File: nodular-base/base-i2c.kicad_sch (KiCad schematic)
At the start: 2 parts, among them U4 TCA9548APWR, U7 SC7A20

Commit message: WIP layout for base
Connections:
- net SDA_C: now reaches U4.10 (SD3)
- net SCL_C: now reaches U4.11 (SC3)
- net GND: now reaches U4.12 (GND)
- net SDA_D: now reaches U4.13 (SD4)
- net SCL_D: now reaches U4.14 (SC4)
- net SDA_E: now reaches U4.15 (SD5)
- net SCL_E: now reaches U4.16 (SC5)
- net SDA_F: now reaches U4.17 (SD6)
- net SCL_F: now reaches U4.18 (SC6)
- net SDA_SYS: now reaches U4.4 (SD0)
- net SCL_SYS: now reaches U4.5 (SC0)
- net SDA_A: now reaches U4.6 (SD1)
- net SCL_A: now reaches U4.7 (SC1)
- net SDA_B: now reaches U4.8 (SD2)
- net SCL_B: now reaches U4.9 (SC2)
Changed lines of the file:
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@@
 (kicad_sch (version 20230121) (generator eeschema)
   (paper "A4")
+  (hierarchical_label "SCL_E" (shape output) (at 123.19 82.55 0) (fields_autoplaced)
+    (effects (font (size 1.27 1.27)) (justify left))
+  )
+  (hierarchical_label "SDA_D" (shape bidirectional) (at 123.19 80.01 0) (fields_autoplaced)
+    (effects (font (size 1.27 1.27)) (justify left))
+  )
+  (hierarchical_label "SCL_SYS" (shape output) (at 123.19 57.15 0) (fields_autoplaced)
+    (effects (font (size 1.27 1.27)) (justify left))
+  )
+  (hierarchical_label "SCL_F" (shape output) (at 123.19 87.63 0) (fields_autoplaced)
+    (effects (font (size 1.27 1.27)) (justify left))
+  )
+  (hierarchical_label "SDA_B" (shape bidirectional) (at 123.19 69.85 0) (fields_autoplaced)
+    (effects (font (size 1.27 1.27)) (justify left))
+  )
+  (hierarchical_label "SCL_B" (shape output) (at 123.19 67.31 0) (fields_autoplaced)
+    (effects (font (size 1.27 1.27)) (justify left))
+  )
+  (hierarchical_label "SDA_C" (shape bidirectional) (at 123.19 74.93 0) (fields_autoplaced)
+    (effects (font (size 1.27 1.27)) (justify left))
+  )
+  (hierarchical_label "SDA_F" (shape bidirectional) (at 123.19 90.17 0) (fields_autoplaced)
+    (effects (font (size 1.27 1.27)) (justify left))
+  )
+  (hierarchical_label "SCL_C" (shape output) (at 123.19 72.39 0) (fields_autoplaced)
+    (effects (font (size 1.27 1.27)) (justify left))
+  )
+  (hierarchical_label "SDA_A" (shape bidirectional) (at 123.19 64.77 0) (fields_autoplaced)
+    (effects (font (size 1.27 1.27)) (justify left))
+  )
+  (hierarchical_label "SDA_SYS" (shape bidirectional) (at 123.19 59.69 0) (fields_autoplaced)
+    (effects (font (size 1.27 1.27)) (justify left))
+  )
+  (hierarchical_label "SCL_D" (shape output) (at 123.19 77.47 0) (fields_autoplaced)
+    (effects (font (size 1.27 1.27)) (justify left))
+  )
+  (hierarchical_label "SDA_E" (shape bidirectional) (at 123.19 85.09 0) (fields_autoplaced)
+    (effects (font (size 1.27 1.27)) (justify left))
+  )
+  (hierarchical_label "SCL_A" (shape output) (at 123.19 62.23 0) (fields_autoplaced)
+    (effects (font (size 1.27 1.27)) (justify left))
+  )
   (symbol (lib_id "Interface_Expansion:TCA9548APWR") (at 113.03 74.93 0) (unit 1)
     (in_bom yes) (on_board yes) (dnp no) (fields_autoplaced)
@@
         )
       )
+    )
+  )
+  (symbol (lib_id "power:GND") (at 113.03 100.33 0) (unit 1)
+    (in_bom yes) (on_board yes) (dnp no) (fields_autoplaced)
+    (property "Reference" "#PWR042" (at 113.03 106.68 0)
+      (effects (font (size 1.27 1.27)) hide)
+    )
+    (property "Value" "GND" (at 113.03 105.41 0)
+      (effects (font (size 1.27 1.27)))
+    )
+    (property "Footprint" "" (at 113.03 100.33 0)
+      (effects (font (size 1.27 1.27)) hide)
+    )
+    (property "Datasheet" "" (at 113.03 100.33 0)
+      (effects (font (size 1.27 1.27)) hide)
+    )
+    (pin "1")
+    (instances
+      (project "nodular-base"
+        (path "/6dcb0502-87e2-4c28-9ce8-81aab8925f06/5ae693f9-48f3-406c-bbdf-b76d81cc71eb"
+          (reference "#PWR042") (unit 1)
+        )
+      )

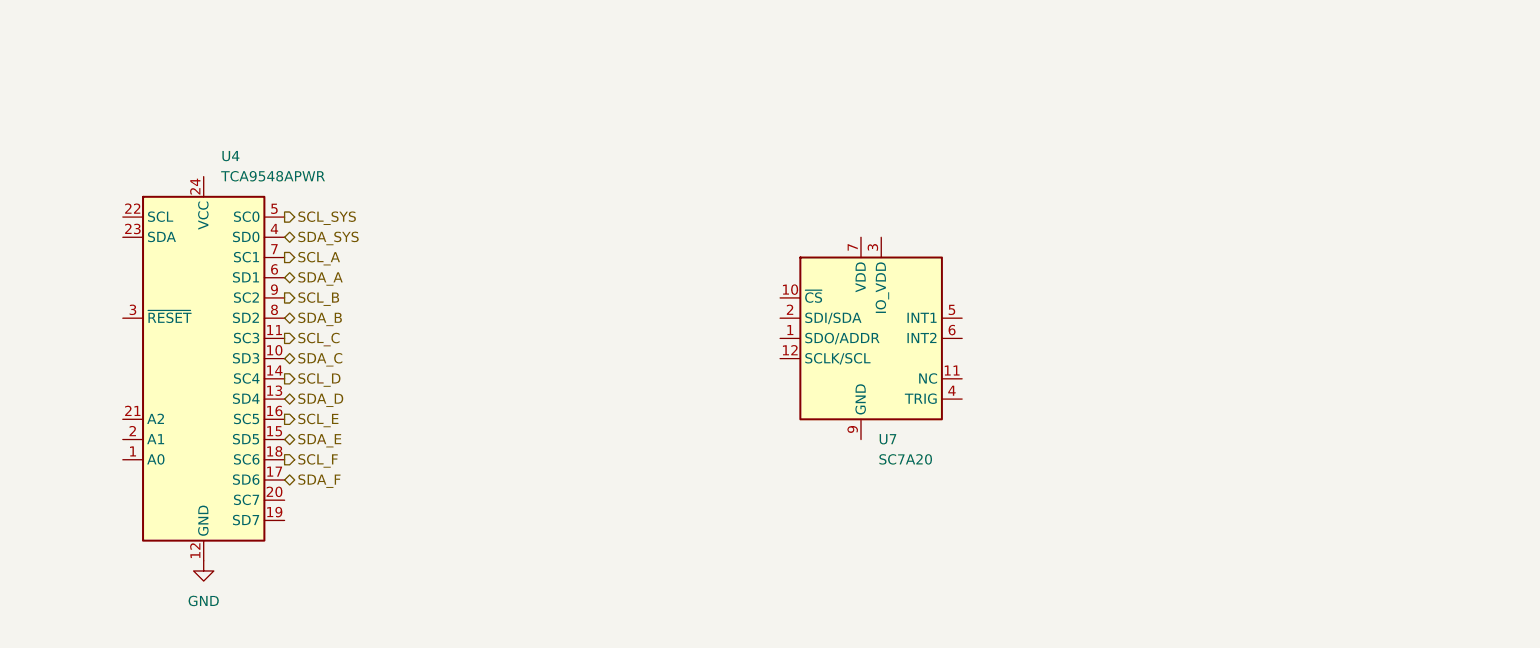
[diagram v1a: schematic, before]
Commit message: Switched from CAN to USB for second USB-C port Added second PD controller and USB mux to allow switching between host and device port Added SOICbite to corner All routing complete Updated pin map, added i2c addresses, soicbit pin mapping, and fpc pinout to document
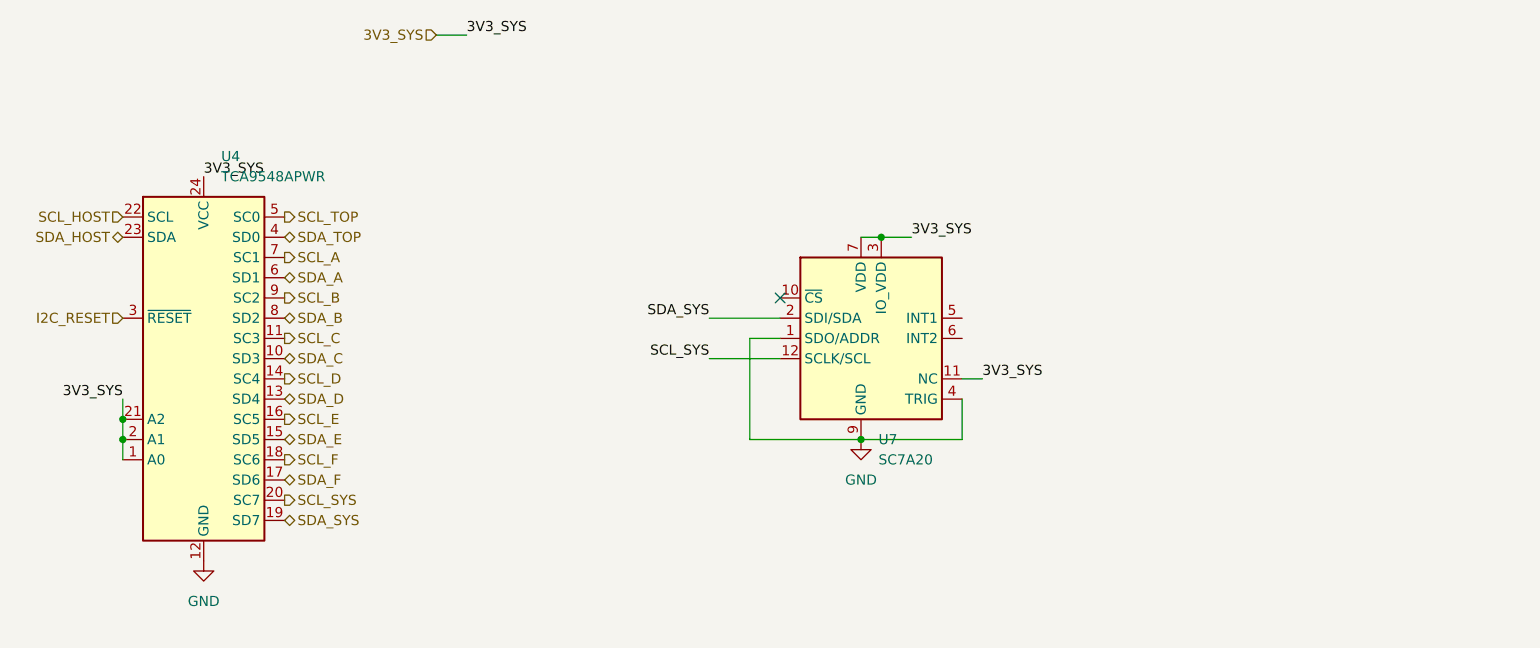
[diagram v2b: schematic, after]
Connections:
- net GND: now also U7.1 (SDO/ADDR), U7.4 (TRIG), U7.9 (GND)
- net SCL_SYS: now also U4.20 (SC7), U7.12 (SCLK/SCL); no longer U4.5 (SC0)
- net SDA_SYS: now also U4.19 (SD7), U7.2 (SDI/SDA); no longer U4.4 (SD0)
- net 3V3_SYS: now reaches U4.1 (A0)
- net 3V3_SYS: now also U4.2 (A1), U4.21 (A2), U4.24 (VCC), U7.11 (NC), U7.3 (IO_VDD), U7.7 (VDD)
- net SCL_HOST: now reaches U4.22 (SCL)
- net SDA_HOST: now reaches U4.23 (SDA)
- net I2C_RESET: now reaches U4.3 (~{RESET})
- new net SCL_TOP: U4.5 (SC0)
- new net SDA_TOP: U4.4 (SD0)
- no-connect marks 0 -> 1
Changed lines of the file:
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@@
 (kicad_sch (version 20230121) (generator eeschema)
   (paper "A4")
+  (junction (at 102.87 85.09) (diameter 0) (color 0 0 0 0)
+  )
+  (junction (at 102.87 82.55) (diameter 0) (color 0 0 0 0)
+  )
+  (junction (at 198.12 59.69) (diameter 0) (color 0 0 0 0)
+  )
+  (junction (at 195.58 85.09) (diameter 0) (color 0 0 0 0)
+  )
+  (no_connect (at 185.42 67.31))
+  (wire (pts (xy 102.87 82.55) (xy 102.87 85.09))
+    (stroke (width 0) (type default))
+  )
+  (wire (pts (xy 198.12 59.69) (xy 201.93 59.69))
+    (stroke (width 0) (type default))
+  )
+  (wire (pts (xy 176.53 74.93) (xy 185.42 74.93))
+    (stroke (width 0) (type default))
+  )
+  (wire (pts (xy 208.28 85.09) (xy 195.58 85.09))
+    (stroke (width 0) (type default))
+  )
+  (wire (pts (xy 176.53 69.85) (xy 185.42 69.85))
+    (stroke (width 0) (type default))
+  )
+  (wire (pts (xy 102.87 80.01) (xy 102.87 82.55))
+    (stroke (width 0) (type default))
+  )
+  (wire (pts (xy 181.61 85.09) (xy 195.58 85.09))
+    (stroke (width 0) (type default))
+  )
+  (wire (pts (xy 195.58 59.69) (xy 198.12 59.69))
+    (stroke (width 0) (type default))
+  )
+  (wire (pts (xy 181.61 72.39) (xy 181.61 85.09))
+    (stroke (width 0) (type default))
+  )
+  (wire (pts (xy 185.42 72.39) (xy 181.61 72.39))
+    (stroke (width 0) (type default))
+  )
+  (wire (pts (xy 102.87 85.09) (xy 102.87 87.63))
+    (stroke (width 0) (type default))
+  )
+  (wire (pts (xy 208.28 77.47) (xy 210.82 77.47))
+    (stroke (width 0) (type default))
+  )
+  (wire (pts (xy 208.28 80.01) (xy 208.28 85.09))
+    (stroke (width 0) (type default))
+  )
+  (wire (pts (xy 142.24 34.29) (xy 146.05 34.29))
+    (stroke (width 0) (type default))
+  )
+  (label "3V3_SYS" (at 113.03 52.07 0) (fields_autoplaced)
+    (effects (font (size 1.27 1.27)) (justify left bottom))
+  )
+  (label "SCL_SYS" (at 176.53 74.93 180) (fields_autoplaced)
+    (effects (font (size 1.27 1.27)) (justify right bottom))
+  )
+  (label "3V3_SYS" (at 102.87 80.01 180) (fields_autoplaced)
+    (effects (font (size 1.27 1.27)) (justify right bottom))
+  )
+  (label "3V3_SYS" (at 201.93 59.69 0) (fields_autoplaced)
+    (effects (font (size 1.27 1.27)) (justify left bottom))
+  )
+  (label "3V3_SYS" (at 210.82 77.47 0) (fields_autoplaced)
+    (effects (font (size 1.27 1.27)) (justify left bottom))
+  )
+  (label "SDA_SYS" (at 176.53 69.85 180) (fields_autoplaced)
+    (effects (font (size 1.27 1.27)) (justify right bottom))
+  )
+  (label "3V3_SYS" (at 146.05 34.29 0) (fields_autoplaced)
+    (effects (font (size 1.27 1.27)) (justify left bottom))
+  )
+  (hierarchical_label "3V3_SYS" (shape input) (at 142.24 34.29 180) (fields_autoplaced)
+    (effects (font (size 1.27 1.27)) (justify right))
+  )
   (hierarchical_label "SCL_E" (shape output) (at 123.19 82.55 0) (fields_autoplaced)
     (effects (font (size 1.27 1.27)) (justify left))
@@
     (effects (font (size 1.27 1.27)) (justify left))
   )
-  (hierarchical_label "SCL_SYS" (shape output) (at 123.19 57.15 0) (fields_autoplaced)
+  (hierarchical_label "SDA_HOST" (shape bidirectional) (at 102.87 59.69 180) (fields_autoplaced)
+    (effects (font (size 1.27 1.27)) (justify right))
+  )
+  (hierarchical_label "SCL_SYS" (shape output) (at 123.19 92.71 0) (fields_autoplaced)
     (effects (font (size 1.27 1.27)) (justify left))
   )
@@
     (effects (font (size 1.27 1.27)) (justify left))
   )
+  (hierarchical_label "I2C_RESET" (shape input) (at 102.87 69.85 180) (fields_autoplaced)
+    (effects (font (size 1.27 1.27)) (justify right))
+  )
   (hierarchical_label "SCL_B" (shape output) (at 123.19 67.31 0) (fields_autoplaced)
     (effects (font (size 1.27 1.27)) (justify left))
@@
     (effects (font (size 1.27 1.27)) (justify left))
   )
+  (hierarchical_label "SCL_HOST" (shape input) (at 102.87 57.15 180) (fields_autoplaced)
+    (effects (font (size 1.27 1.27)) (justify right))
+  )
+  (hierarchical_label "SCL_TOP" (shape output) (at 123.19 57.15 0) (fields_autoplaced)
+    (effects (font (size 1.27 1.27)) (justify left))
+  )
   (hierarchical_label "SDA_F" (shape bidirectional) (at 123.19 90.17 0) (fields_autoplaced)
     (effects (font (size 1.27 1.27)) (justify left))
@@
     (effects (font (size 1.27 1.27)) (justify left))
   )
-  (hierarchical_label "SDA_SYS" (shape bidirectional) (at 123.19 59.69 0) (fields_autoplaced)
+  (hierarchical_label "SDA_SYS" (shape bidirectional) (at 123.19 95.25 0) (fields_autoplaced)
     (effects (font (size 1.27 1.27)) (justify left))
   )
@@
   )
   (hierarchical_label "SDA_E" (shape bidirectional) (at 123.19 85.09 0) (fields_autoplaced)
+    (effects (font (size 1.27 1.27)) (justify left))
+  )
+  (hierarchical_label "SDA_TOP" (shape bidirectional) (at 123.19 59.69 0) (fields_autoplaced)
     (effects (font (size 1.27 1.27)) (justify left))
   )
@@
         )
       )
+    )
+  )
+  (symbol (lib_id "power:GND") (at 195.58 85.09 0) (unit 1)
+    (in_bom yes) (on_board yes) (dnp no) (fields_autoplaced)
+    (property "Reference" "#PWR050" (at 195.58 91.44 0)
+      (effects (font (size 1.27 1.27)) hide)
+    )
+    (property "Value" "GND" (at 195.58 90.17 0)
+      (effects (font (size 1.27 1.27)))
+    )
+    (property "Footprint" "" (at 195.58 85.09 0)
+      (effects (font (size 1.27 1.27)) hide)
+    )
+    (property "Datasheet" "" (at 195.58 85.09 0)
+      (effects (font (size 1.27 1.27)) hide)
+    )
+    (pin "1")
+    (instances
+      (project "nodular-base"
+        (path "/6dcb0502-87e2-4c28-9ce8-81aab8925f06/5ae693f9-48f3-406c-bbdf-b76d81cc71eb"
+          (reference "#PWR050") (unit 1)
+        )
+      )

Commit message: Add hole Add decoupling caps, pullups, and voltage dividers Set current limit on PMIC Determine battery attachment angle Update BOM and pinouts
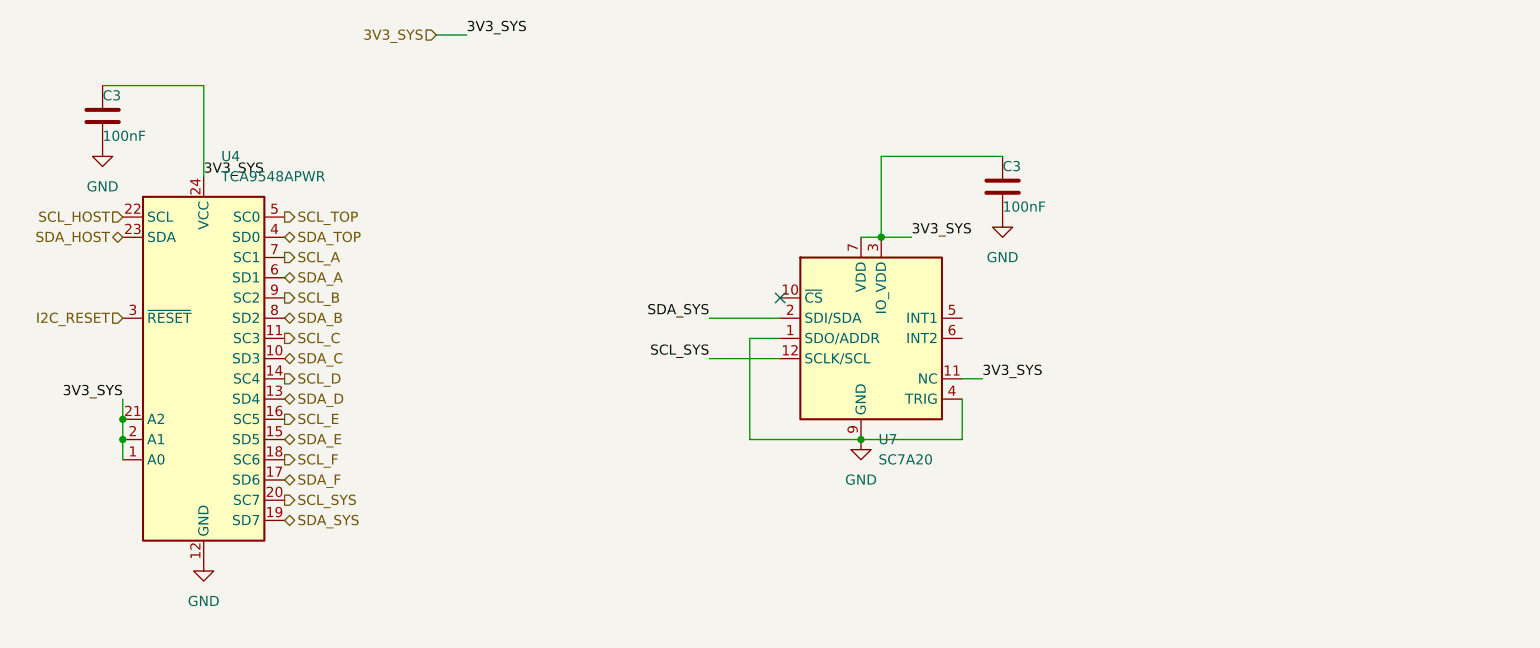
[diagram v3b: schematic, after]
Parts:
- added C3 (x2): 100nF, Capacitor_SMD:C_0402_1005Metric, symbol Device:C
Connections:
- net 3V3_SYS: now also C3.1, C3.1
- net GND: now also C3.2, C3.2
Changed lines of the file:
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@@
+    (stroke (width 0) (type default))
+  )
+  (wire (pts (xy 113.03 40.64) (xy 100.33 40.64))
     (stroke (width 0) (type default))
   )
@@
     (stroke (width 0) (type default))
   )
+  (wire (pts (xy 213.36 49.53) (xy 198.12 49.53))
+    (stroke (width 0) (type default))
+  )
   (wire (pts (xy 102.87 80.01) (xy 102.87 82.55))
     (stroke (width 0) (type default))
@@
     (stroke (width 0) (type default))
   )
+  (wire (pts (xy 113.03 52.07) (xy 113.03 40.64))
+    (stroke (width 0) (type default))
+  )
   (wire (pts (xy 195.58 59.69) (xy 198.12 59.69))
+    (stroke (width 0) (type default))
+  )
+  (wire (pts (xy 198.12 49.53) (xy 198.12 59.69))
     (stroke (width 0) (type default))
   )
@@
     )
   )
+  (symbol (lib_id "Device:C") (at 213.36 53.34 0) (unit 1)
+    (in_bom yes) (on_board yes) (dnp no)
+    (property "Reference" "C3" (at 213.36 50.8 0)
+      (effects (font (size 1.27 1.27)) (justify left))
+    )
+    (property "Value" "100nF" (at 213.36 55.88 0)
+      (effects (font (size 1.27 1.27)) (justify left))
+    )
+    (property "Footprint" "Capacitor_SMD:C_0402_1005Metric" (at 214.3252 57.15 0)
+      (effects (font (size 1.27 1.27)) hide)
+    )
+    (property "Datasheet" "~" (at 213.36 53.34 0)
+      (effects (font (size 1.27 1.27)) hide)
+    )
+    (pin "1")
+    (pin "2")
+    (instances
+      (project "nodular-base"
+        (path "/6dcb0502-87e2-4c28-9ce8-81aab8925f06"
+          (reference "C3") (unit 1)
+        )
+        (path "/6dcb0502-87e2-4c28-9ce8-81aab8925f06/5ae693f9-48f3-406c-bbdf-b76d81cc71eb"
+          (reference "C42") (unit 1)
+        )
+      )
+    )
+  )
+  (symbol (lib_id "Device:C") (at 100.33 44.45 0) (unit 1)
+    (in_bom yes) (on_board yes) (dnp no)
+    (property "Reference" "C3" (at 100.33 41.91 0)
+      (effects (font (size 1.27 1.27)) (justify left))
+    )
+    (property "Value" "100nF" (at 100.33 46.99 0)
+      (effects (font (size 1.27 1.27)) (justify left))
+    )
+    (property "Footprint" "Capacitor_SMD:C_0402_1005Metric" (at 101.2952 48.26 0)
+      (effects (font (size 1.27 1.27)) hide)
+    )
+    (property "Datasheet" "~" (at 100.33 44.45 0)
+      (effects (font (size 1.27 1.27)) hide)
+    )
+    (pin "1")
+    (pin "2")
+    (instances
+      (project "nodular-base"
+        (path "/6dcb0502-87e2-4c28-9ce8-81aab8925f06"
+          (reference "C3") (unit 1)
+        )
+        (path "/6dcb0502-87e2-4c28-9ce8-81aab8925f06/5ae693f9-48f3-406c-bbdf-b76d81cc71eb"
+          (reference "C16") (unit 1)
+        )
+      )
+    )
+  )
+  (symbol (lib_id "power:GND") (at 213.36 57.15 0) (unit 1)
+    (in_bom yes) (on_board yes) (dnp no) (fields_autoplaced)
+    (property "Reference" "#PWR061" (at 213.36 63.5 0)
+      (effects (font (size 1.27 1.27)) hide)
+    )
+    (property "Value" "GND" (at 213.36 62.23 0)
+      (effects (font (size 1.27 1.27)))
+    )
+    (property "Footprint" "" (at 213.36 57.15 0)
+      (effects (font (size 1.27 1.27)) hide)
+    )
+    (property "Datasheet" "" (at 213.36 57.15 0)
+      (effects (font (size 1.27 1.27)) hide)
+    )
+    (pin "1")
+    (instances
+      (project "nodular-base"
+        (path "/6dcb0502-87e2-4c28-9ce8-81aab8925f06/5ae693f9-48f3-406c-bbdf-b76d81cc71eb"
+          (reference "#PWR061") (unit 1)
+        )
+      )
+    )
+  )
   (symbol (lib_id "power:GND") (at 195.58 85.09 0) (unit 1)
     (in_bom yes) (on_board yes) (dnp no) (fields_autoplaced)
@@
         )
       )
+    )
+  )
+  (symbol (lib_id "power:GND") (at 100.33 48.26 0) (unit 1)
+    (in_bom yes) (on_board yes) (dnp no) (fields_autoplaced)
+    (property "Reference" "#PWR062" (at 100.33 54.61 0)
+      (effects (font (size 1.27 1.27)) hide)
+    )
+    (property "Value" "GND" (at 100.33 53.34 0)
+      (effects (font (size 1.27 1.27)))
+    )
+    (property "Footprint" "" (at 100.33 48.26 0)
+      (effects (font (size 1.27 1.27)) hide)
+    )
+    (property "Datasheet" "" (at 100.33 48.26 0)
+      (effects (font (size 1.27 1.27)) hide)
+    )
+    (pin "1")
+    (instances
+      (project "nodular-base"
+        (path "/6dcb0502-87e2-4c28-9ce8-81aab8925f06/5ae693f9-48f3-406c-bbdf-b76d81cc71eb"
+          (reference "#PWR062") (unit 1)
+        )
+      )

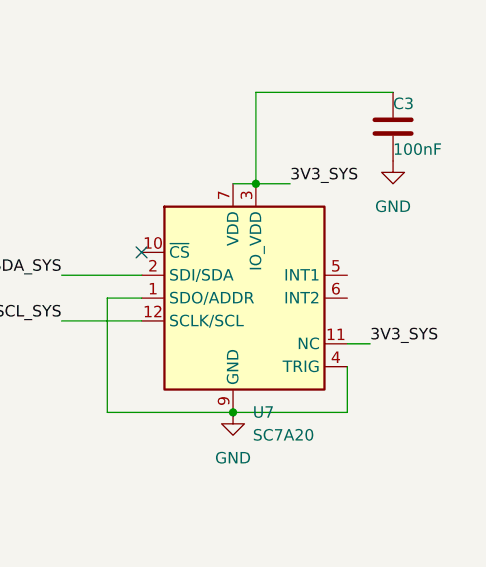
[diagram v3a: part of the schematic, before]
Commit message: Add VCONN support and load switch with 1.5A current limit on host port Add accelerometer interrupt connection Update BOM with important capacitor and inductor PNs and costings
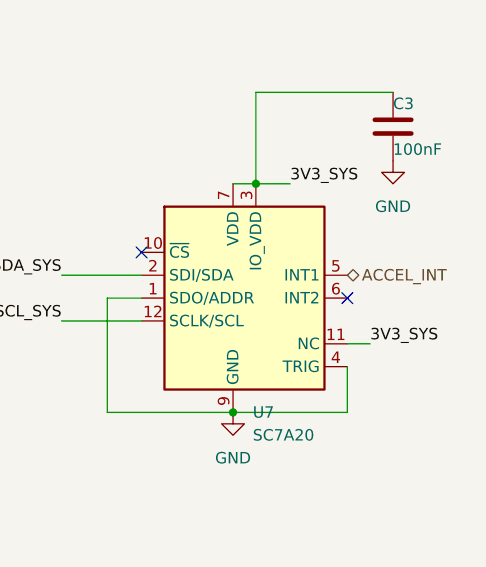
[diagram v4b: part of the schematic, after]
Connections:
- net ACCEL_INT: now reaches U7.5 (INT1)
- no-connect marks 1 -> 2
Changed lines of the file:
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@@
   (junction (at 195.58 85.09) (diameter 0) (color 0 0 0 0)
   )
+  (no_connect (at 208.28 72.39))
   (no_connect (at 185.42 67.31))
   (wire (pts (xy 102.87 82.55) (xy 102.87 85.09))
@@
     (effects (font (size 1.27 1.27)) (justify right))
   )
+  (hierarchical_label "ACCEL_INT" (shape bidirectional) (at 208.28 69.85 0) (fields_autoplaced)
+    (effects (font (size 1.27 1.27)) (justify left))
+  )
   (hierarchical_label "SCL_B" (shape output) (at 123.19 67.31 0) (fields_autoplaced)
